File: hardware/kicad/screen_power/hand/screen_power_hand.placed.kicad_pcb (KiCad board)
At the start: 2 copper layers, 68 x 76 mm, 41 parts, among them J1 AUX 5V INPUT, J101 PI USB / XH4, J102 TOUCH / XH4, J103 SCREEN 1 POWER, J2 GPIO17 / GND, J201 PI USB / XH4, J202 TOUCH / XH4, J203 SCREEN 2 POWER, K101 IM02TS, K201 IM02TS, Q1 2N3904, Q101 2N7000, Q2 2N3906, Q201 2N7000, Q3 SUP70101EL, Q4 SUP70101EL

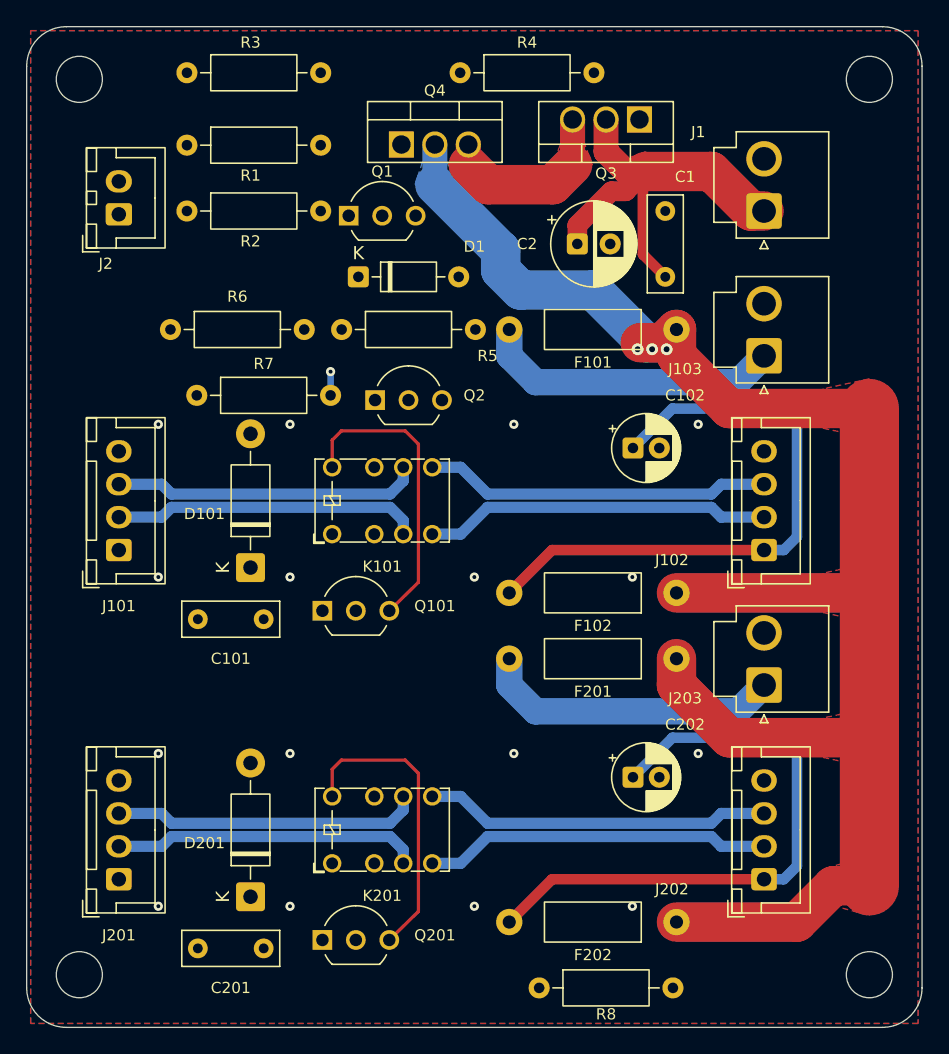
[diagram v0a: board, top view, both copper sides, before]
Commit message: fix(hardware): strengthen screen gate drive and finish PCB copper
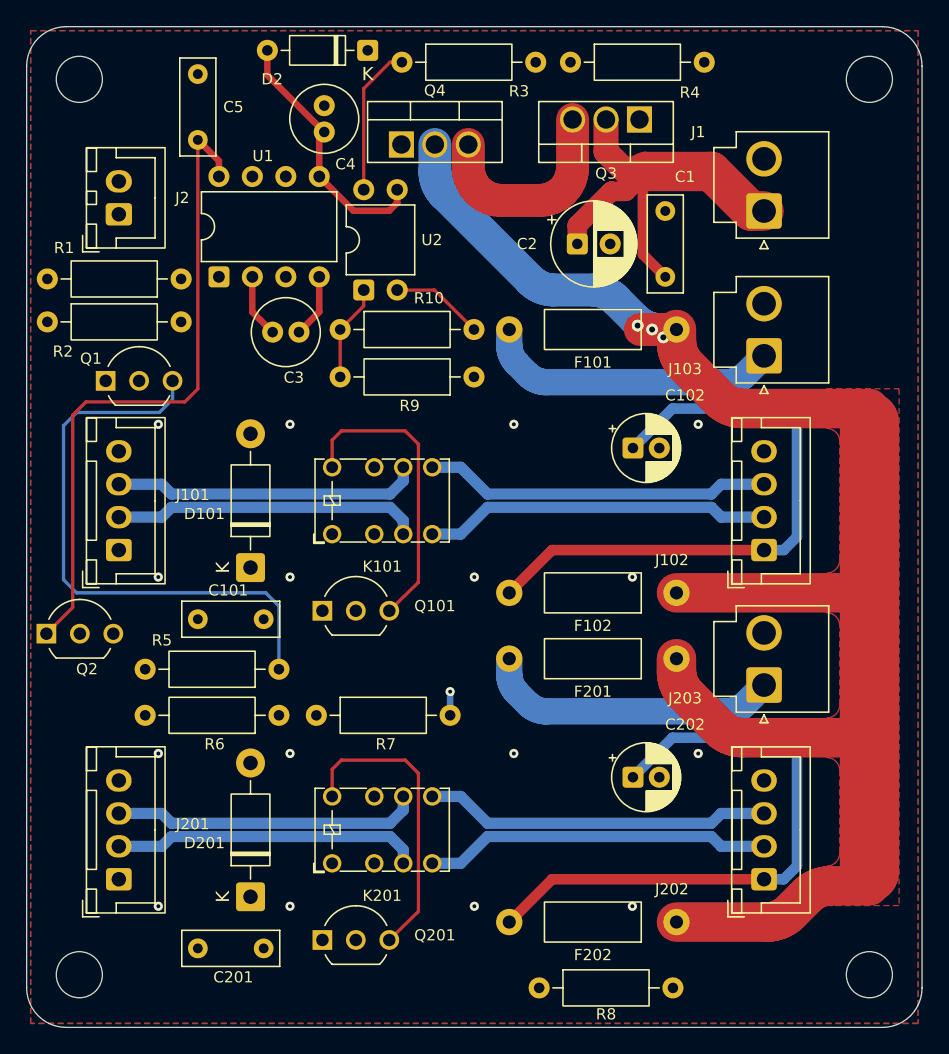
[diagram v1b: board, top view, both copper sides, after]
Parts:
- removed D1: 1N4148, D_DO-35_SOD27_P7.62mm_Horizontal
- added C3: 10uF 25V bipolar, C_Radial_D5.0mm_H11.0mm_P2.00mm, F.Cu at (18.7, 23.2)
- added C4: 10uF 25V bipolar, C_Radial_D5.0mm_H11.0mm_P2.00mm, F.Cu at (22.6, 6.00)
- added C5: 100nF 63V, C_Rect_L7.2mm_W2.5mm_P5.00mm, F.Cu at (13.0, 8.60)
- added D2: BAT85S, D_DO-35_SOD27_P7.62mm_Horizontal, F.Cu at (25.9, 1.80)
- added R10: 10k 1%, R_Axial_DIN0207_L6.3mm_D2.5mm_P10.16mm_Horizontal, F.Cu at (23.8, 23.0)
- added R9: 2.4k 1%, R_Axial_DIN0207_L6.3mm_D2.5mm_P10.16mm_Horizontal, F.Cu at (34.0, 26.6)
- added U1: LMC7660IN, DIP-8_W7.62mm, F.Cu at (14.6, 19.0)
- added U2: TLP627M, DIP-4_W7.62mm, F.Cu at (25.6, 20.0)
- Q101, Q201: value 2N7000 -> TN0702
- R4: value 330k 1% -> 22k 1%
- moved Q2 30.6 mm to (1.50, 46.1)
- moved R6 30.4 mm to (19.2, 52.3), turned to 180 degrees
- moved R5 26.2 mm to (19.2, 48.8), turned to 180 degrees
- moved R7 25.9 mm to (22.0, 52.3)
- moved Q1 22.3 mm to (6.00, 26.9)
- moved R3 16.3 mm to (28.5, 2.70)
- moved R2 13.5 mm to (1.57, 22.4)
- moved R1 10.2 mm to (11.7, 19.2), turned to 180 degrees
- moved R4 8.42 mm to (41.3, 2.70)
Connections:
- R3 pad 1: CONTROL_SINK -> GATE_SINK
- R5 pad 1: BUFFER_SINK -> CONTROL_SINK
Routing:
- net CONTROL_SINK: track 0.00 -> 51.3 mm
- net AUX_5V: track 33.4 -> 83.5 mm
- net NEG_5V: track 0.00 -> 19.8 mm
- net GATE_SINK: track 0.00 -> 11.4 mm
- net GATE_LED: track 0.00 -> 7.34 mm
- net SWITCHED_5V: track 134.1 -> 128.9 mm
- net PUMP_CAP_PLUS: track 0.00 -> 4.84 mm
- net PUMP_CAP_MINUS: track 0.00 -> 4.84 mm
- net COMMON_SOURCE: track 14.2 -> 16.2 mm
- removed copper zone on F.Cu, net COMMON_SOURCE
- removed copper zone on B.Cu, net SWITCHED_5V
